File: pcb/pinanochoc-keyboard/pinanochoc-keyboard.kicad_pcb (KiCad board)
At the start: 2 copper layers, 146 x 140.8 mm, 75 parts, among them J1 AudioJack4, J2 Conn_02x04_Top_Bottom, J3 Conn_02x02_Top_Bottom, SW1 SW_Push, SW10 SW_Push, SW11 SW_Push, SW12 SW_Push, SW13 SW_Push, SW14 SW_Push, SW15 SW_Push, SW16 SW_Push_Dual_x2, SW17 SW_Push, SW18 SW_Push, SW19 SW_Push, SW2 SW_Push, SW20 SW_Push, SW21 SW_Push_Dual_x2, SW22 SW_Push, SW23 SW_Push, SW24 SW_Push, SW25 SW_Push, SW26 SW_Push_Dual_x2, SW27 SW_Push, SW28 SW_Push, SW29 SW_Push, SW3 SW_Push, SW30 SW_Push, SW31 SW_Push_Dual_x2, SW32 Rotary_Encoder_Switch, SW33 SW_Push, SW4 SW_Push, SW5 SW_Push, SW6 SW_Push, SW7 SW_Push, SW8 SW_Push, SW9 SW_Push, U1 Pico

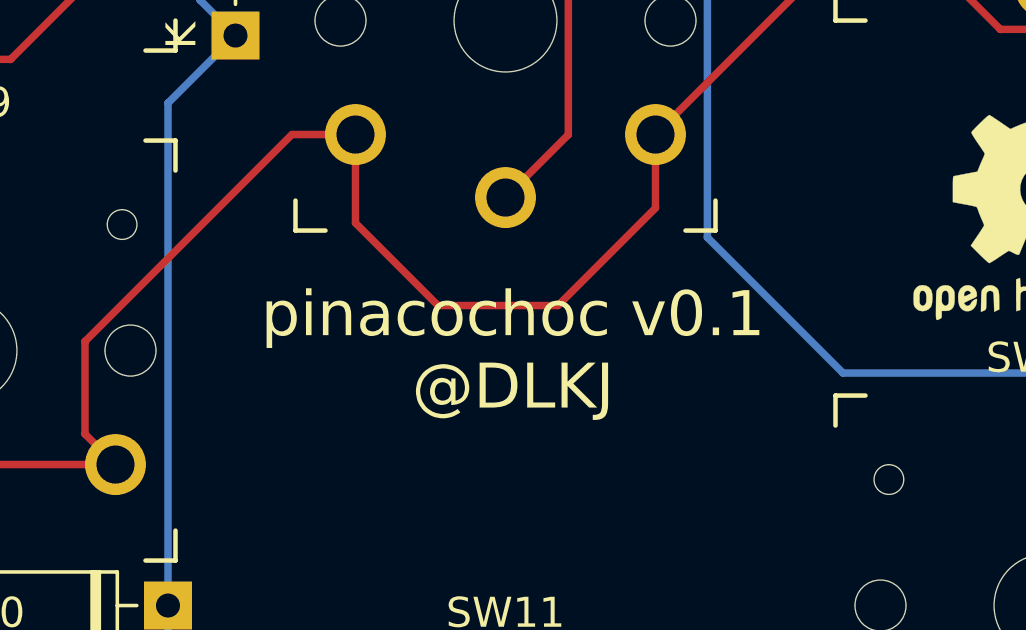
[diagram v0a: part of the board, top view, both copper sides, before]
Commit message: rename pinanococ to pinanochoc and fix typo on silk
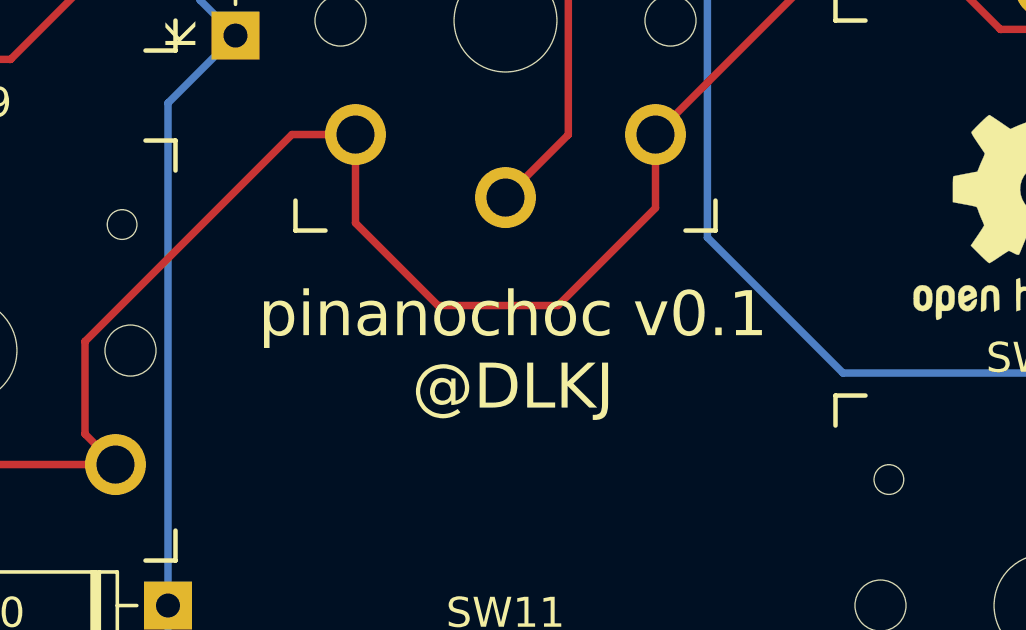
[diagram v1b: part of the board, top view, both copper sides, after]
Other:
- board text added: "pinanochoc v0.1 @DLKJ"
- board text removed: "pinacochoc v0.1 @DLKJ"
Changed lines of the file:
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@@
     )
   )
-  (gr_text "pinacochoc v0.1\n@DLKJ" (at 68.5 102.25) (layer B.SilkS)
+  (gr_text "pinanochoc v0.1\n@DLKJ" (at 68.5 102.25) (layer B.SilkS)
     (effects (font (size 1.5 1.5) (thickness 0.15)) (justify mirror))
   )
-  (gr_text "pinacochoc v0.1\n@DLKJ" (at 68.75 102.5) (layer F.SilkS)
+  (gr_text "pinanochoc v0.1\n@DLKJ" (at 68.75 102.5) (layer F.SilkS)
     (effects (font (size 1.5 1.5) (thickness 0.15)))
   )
